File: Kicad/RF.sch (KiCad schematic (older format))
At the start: 1 part, among them P1 nRF24l01

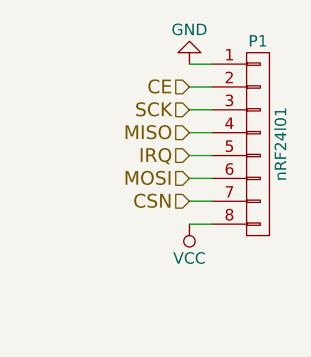
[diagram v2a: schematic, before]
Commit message: Circuito de cargador modificado. A los demás les agregué capacitor en la alimentación, pines sin conexión y cambié BATT- por GND
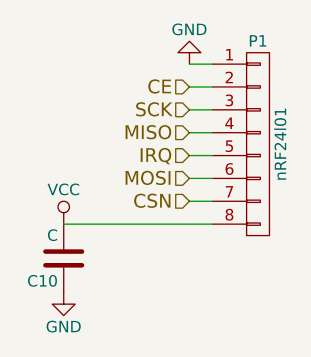
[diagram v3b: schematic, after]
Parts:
- added C10: C, symbol C
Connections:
- net GND: now also C10.1
- net VCC: now also C10.2
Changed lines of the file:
@@
 $EndComp
 $Comp
-L GND #PWR11
+L GND #PWR14
 U 1 1 57DD9164
 P 4850 3000
-F 0 "#PWR11" H 4850 2750 50  0001 C CNN
+F 0 "#PWR14" H 4850 2750 50  0001 C CNN
 F 1 "GND" H 4850 2850 50  0000 C CNN
 F 2 "" H 4850 3000 50  0000 C CNN
@@
 L VCC #PWR12
 U 1 1 57DD917A
-P 4850 3700
-F 0 "#PWR12" H 4850 3550 50  0001 C CNN
-F 1 "VCC" H 4850 3850 50  0000 C CNN
-F 2 "" H 4850 3700 50  0000 C CNN
-F 3 "" H 4850 3700 50  0000 C CNN
-	1    4850 3700
-	-1   0    0    1
+P 4300 3700
+F 0 "#PWR12" H 4300 3550 50  0001 C CNN
+F 1 "VCC" H 4300 3850 50  0000 C CNN
+F 2 "" H 4300 3700 50  0000 C CNN
+F 3 "" H 4300 3700 50  0000 C CNN
+	1    4300 3700
+	1    0    0    -1
 $EndComp
 Text HLabel 4850 3100 0    60   Input ~ 0
@@
 Wire Wire Line
 	4850 3600 4950 3600
+$Comp
+L C C10
+U 1 1 57FAB4AD
+P 4300 3850
+F 0 "C10" H 4325 3950 50  0000 L CNN
+F 1 "C" H 4325 3750 50  0000 L CNN
+F 2 "" H 4338 3700 50  0000 C CNN
+F 3 "" H 4300 3850 50  0000 C CNN
+	1    4300 3850
+	-1   0    0    1
+$EndComp
+$Comp
+L GND #PWR13
+U 1 1 57FAB5CE
+P 4300 4000
+F 0 "#PWR13" H 4300 3750 50  0001 C CNN
+F 1 "GND" H 4300 3850 50  0000 C CNN
+F 2 "" H 4300 4000 50  0000 C CNN
+F 3 "" H 4300 4000 50  0000 C CNN
+	1    4300 4000
+	1    0    0    -1
+$EndComp
 Wire Wire Line
-	4850 3700 4950 3700
+	4950 3700 4300 3700
 $EndSCHEMATC

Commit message: Agregados footprints de C_0805 y R_0805 y asociados a resistencias y capacitores del esquemático
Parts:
- C10: footprint (none) -> EMG:C_0805
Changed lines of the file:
@@
 F 0 "C10" H 4325 3950 50  0000 L CNN
 F 1 "C" H 4325 3750 50  0000 L CNN
-F 2 "" H 4338 3700 50  0001 C CNN
+F 2 "EMG:C_0805" H 4338 3700 50  0001 C CNN
 F 3 "" H 4300 3850 50  0000 C CNN
 	1    4300 3850

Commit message: Agregados footprints de pin headers para elementos faltantes (falta USB)
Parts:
- P1: footprint (none) -> EMG:Pin_Header_Straight_1x08_Pitch1.27mm
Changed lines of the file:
@@
 F 0 "P1" H 5150 3800 50  0000 C CNN
 F 1 "nRF24l01" V 5250 3350 50  0000 C CNN
-F 2 "" H 5150 3350 50  0001 C CNN
+F 2 "EMG:Pin_Header_Straight_1x08_Pitch1.27mm" H 5150 3350 50  0001 C CNN
 F 3 "" H 5150 3350 50  0000 C CNN
 	1    5150 3350
@@
 $EndComp
 $Comp
-L GND #PWR15
+L GND #PWR013
 U 1 1 57DD9164
 P 4850 3000
-F 0 "#PWR15" H 4850 2750 50  0001 C CNN
+F 0 "#PWR013" H 4850 2750 50  0001 C CNN
 F 1 "GND" H 4850 2850 50  0000 C CNN
 F 2 "" H 4850 3000 50  0000 C CNN
@@
 $EndComp
 $Comp
-L VCC #PWR13
+L VCC #PWR014
 U 1 1 57DD917A
 P 4300 3700
-F 0 "#PWR13" H 4300 3550 50  0001 C CNN
+F 0 "#PWR014" H 4300 3550 50  0001 C CNN
 F 1 "VCC" H 4300 3850 50  0000 C CNN
 F 2 "" H 4300 3700 50  0000 C CNN
@@
 $EndComp
 $Comp
-L GND #PWR14
+L GND #PWR015
 U 1 1 57FAB5CE
 P 4300 4000
-F 0 "#PWR14" H 4300 3750 50  0001 C CNN
+F 0 "#PWR015" H 4300 3750 50  0001 C CNN
 F 1 "GND" H 4300 3850 50  0000 C CNN
 F 2 "" H 4300 4000 50  0000 C CNN
